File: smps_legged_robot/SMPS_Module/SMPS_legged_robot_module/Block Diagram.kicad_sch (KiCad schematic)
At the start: 0 parts

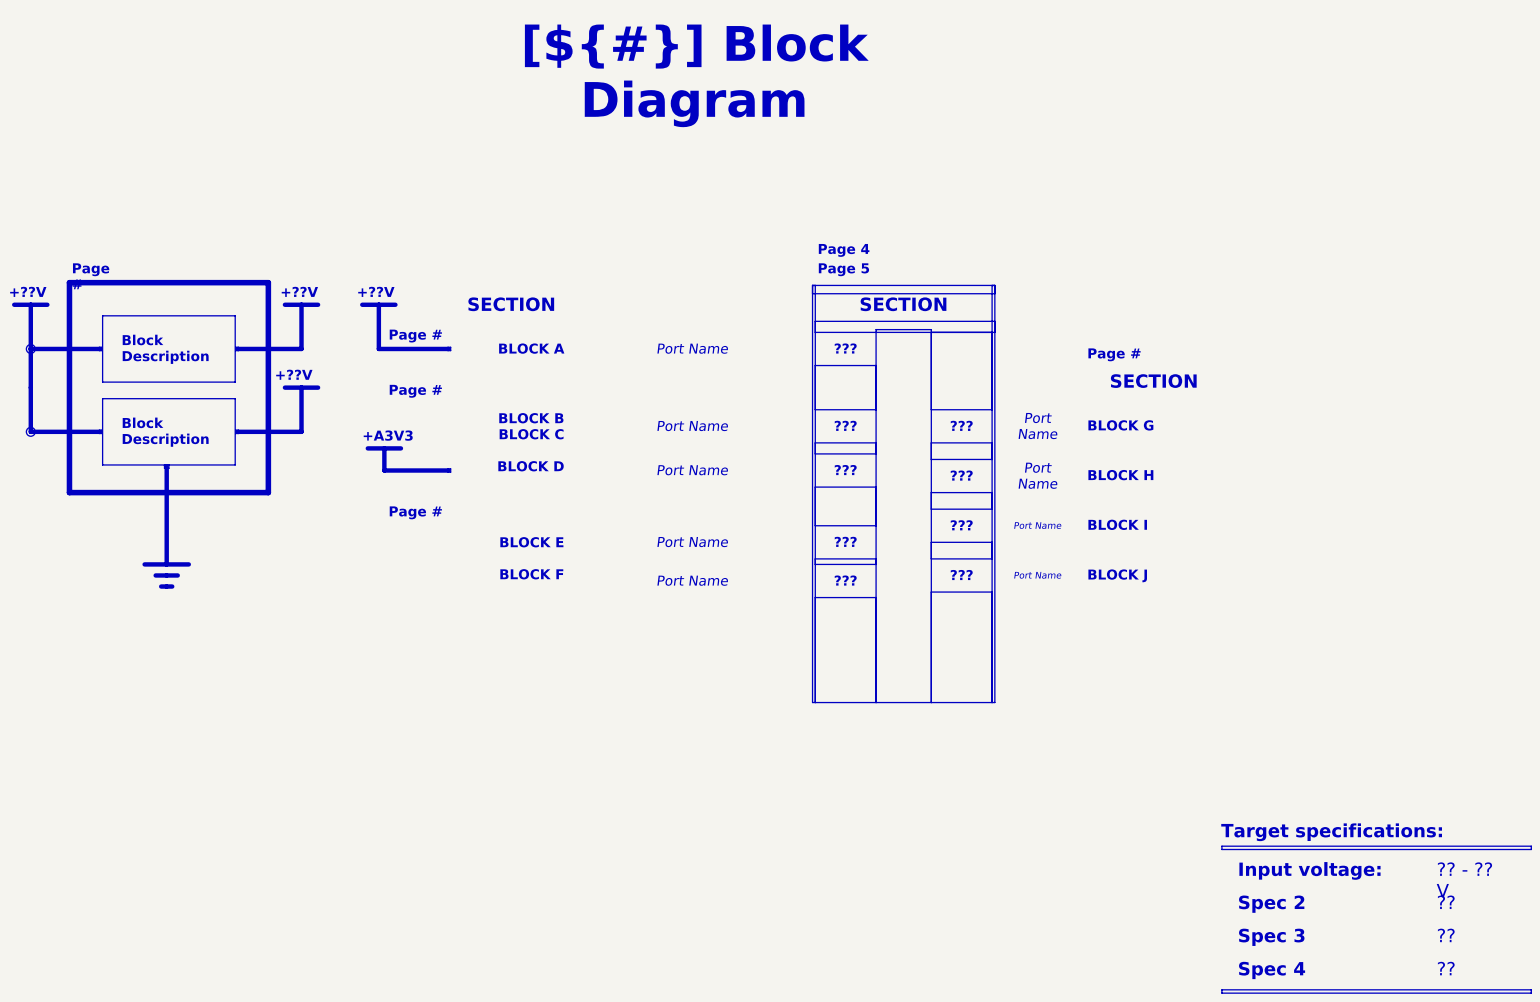
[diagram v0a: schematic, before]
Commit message: Buck module finished pending review
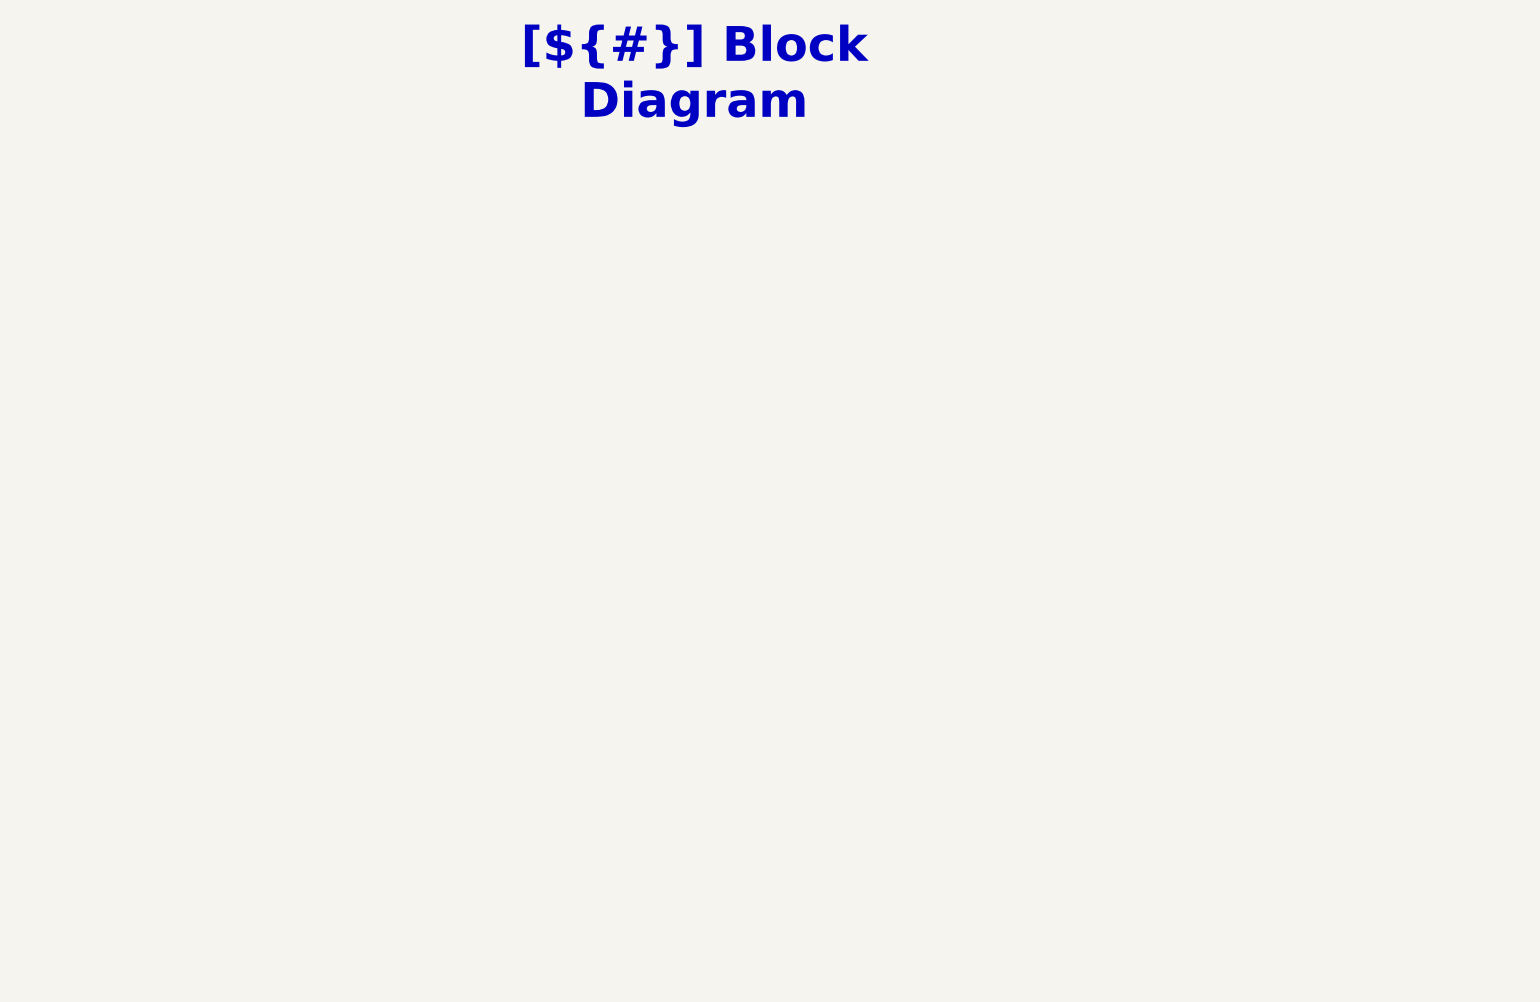
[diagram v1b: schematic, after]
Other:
- note removed: "+??V"
- note removed: "+A3V3"
